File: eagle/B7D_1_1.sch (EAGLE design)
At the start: 11 parts, among them IC1 4511N, X1 In, X3 Out A, X4 Out B

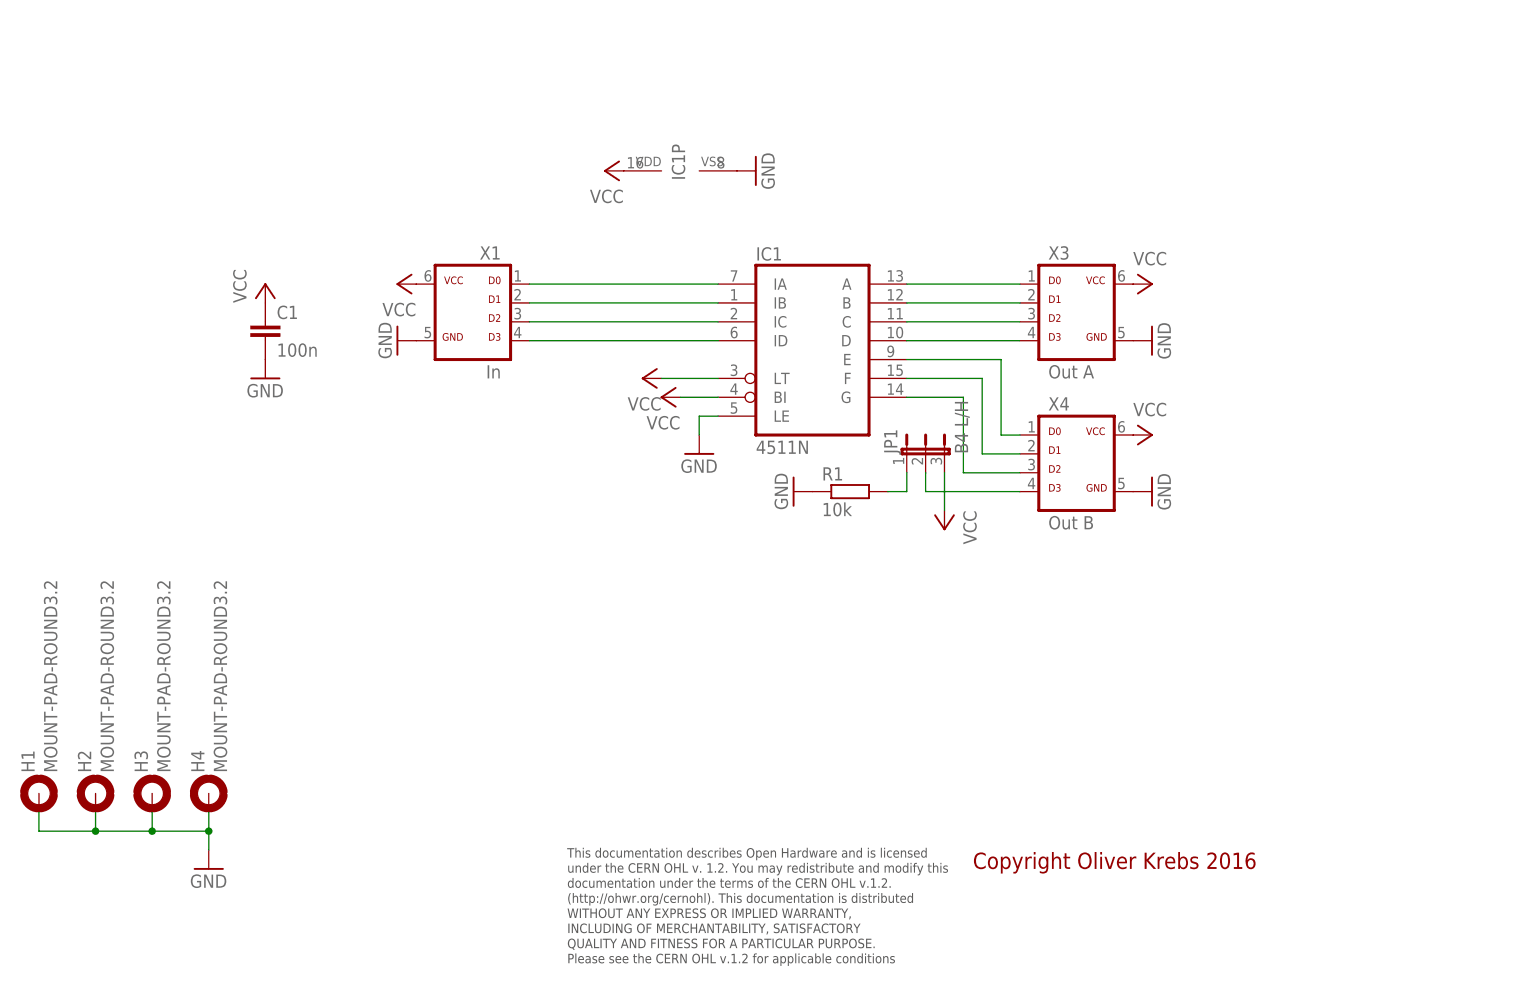
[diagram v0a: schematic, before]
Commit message: Add new tetra-Board and arduino files
Add AMP_1_0, AVC_1_0, D18_1_1, IOP_1_2, MIC_1_0, PIN_1_1, POT_1_0, PWA_1_0, PWR_1_0, RGF 2.0, SOC_2_0, VLT_1_0
Add mex_nano_shield_keyboard, mex_nano_shied_numbers

New arduino projects
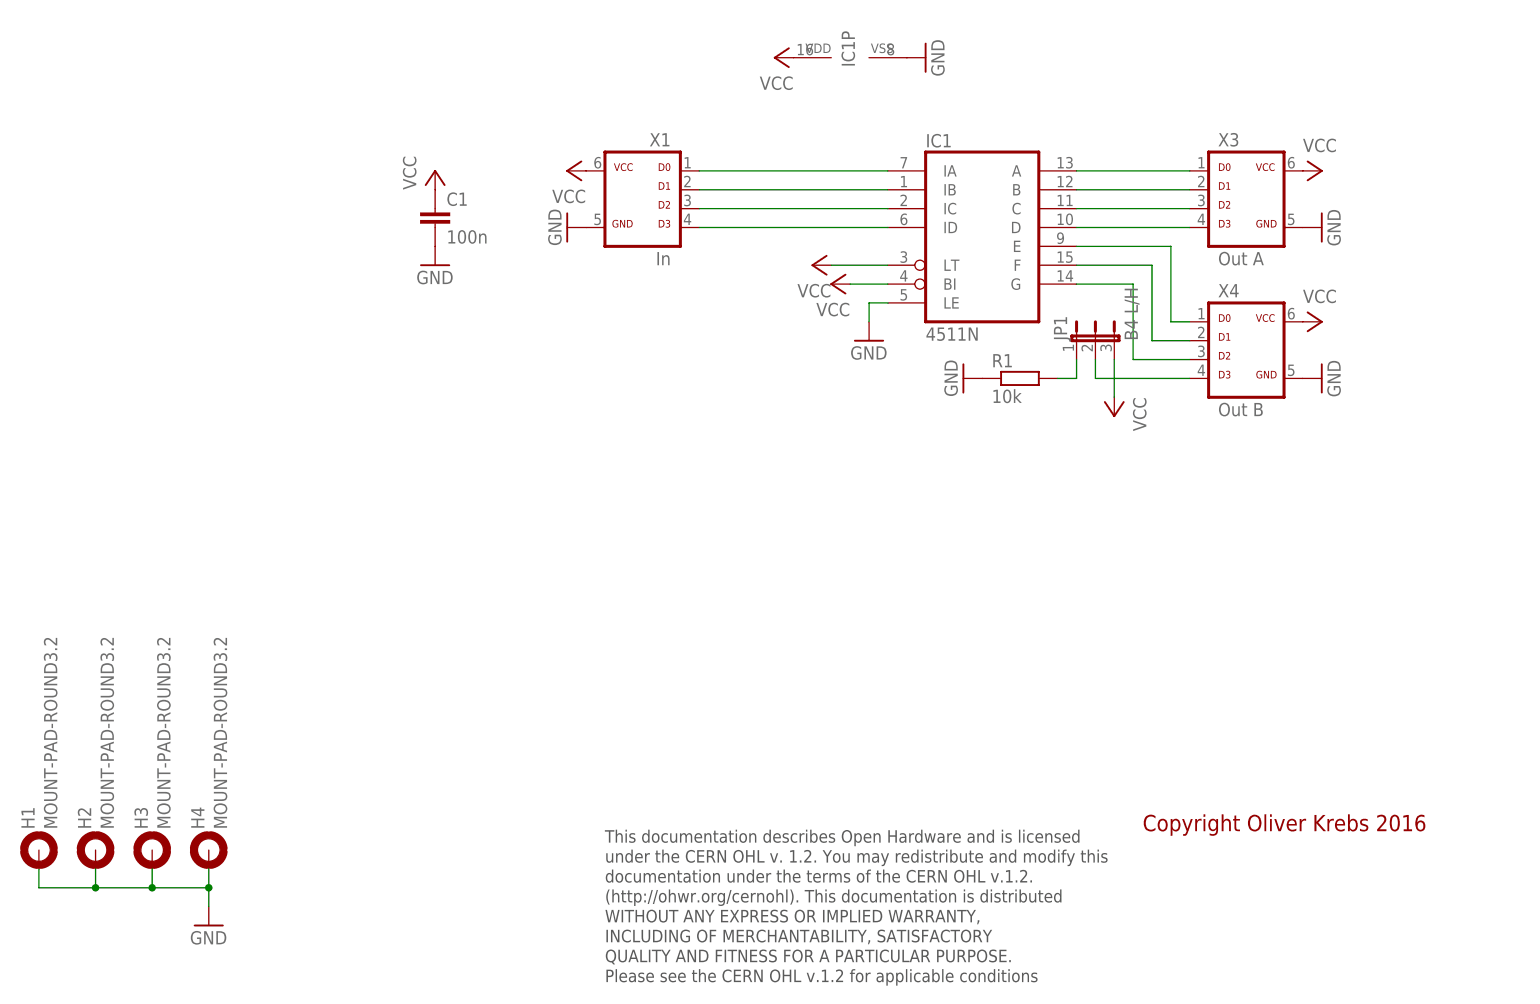
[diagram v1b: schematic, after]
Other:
- moved on the sheet: C1, H1, H2, H3, H4, IC1, IC1P, JP1, R1, X1, X3, X4
